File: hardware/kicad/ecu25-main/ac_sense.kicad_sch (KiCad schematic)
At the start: 82 parts, among them J5 Screw_Terminal_GEN, J6 Screw_Terminal_MAINS, J7 Screw_Terminal_CT, U10 MCP6002, U8 MCP6002, U9 MCP6002

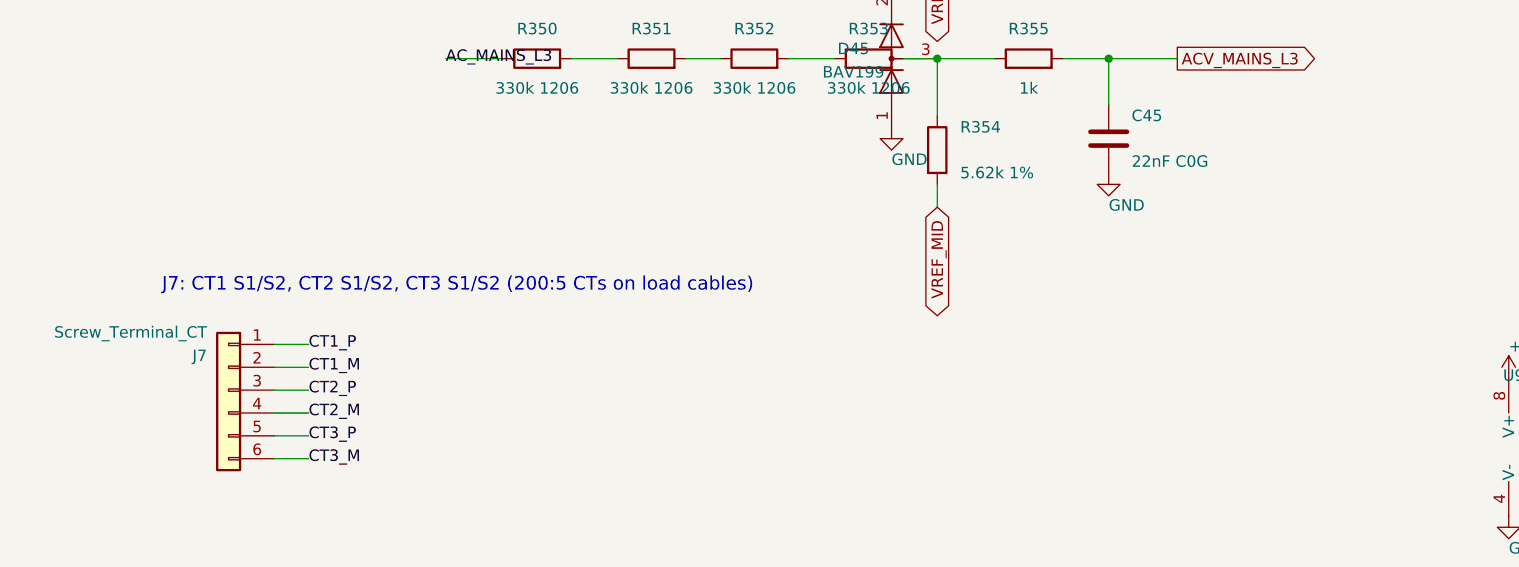
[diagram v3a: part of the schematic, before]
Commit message: Fix firmware SME findings: two criticals in the AC/Modbus interaction
Both criticals needed two modules read together to see.

C1 — a routine Modbus poll could start the engine.
plat_rs485_tx() busy-waited on TXE/TC for the whole response: 26.6 ms for the
51-byte reply to a full input-register read at 19200 baud. The main loop is
the only thing draining the ADC ring, and the ring held 8 sets = 2.5 ms, so
it lapped ten times over with no overrun flag. ac_sense indexes zero
crossings by SAMPLE NUMBER, so a hole in the stream reads as time that did
not pass and comes straight out as a frequency error: a master reading all 23
registers at 10 Hz pinned mains_hz at 53.3 Hz, outside amf_mains_healthy()'s
47-53 window, on every tick. After mains_fail_qualify_ms the controller
declares a mains failure, starts the engine and transfers load. A 12.5 ms
hole crosses the generator frequency trips in both directions.

Fixed three ways, because any one alone is a single point of failure:
- USART3 TX is interrupt-driven; DE still drops on TC, not TXE
- the ring is 64 sets (20 ms) instead of 8
- DMA transfer-complete now counts wraps, so overrun is DETECTABLE (NDTR
  alone is an index and cannot tell "empty" from "lapped exactly once"), and
  the runtime discards the part-built window rather than publishing a
  confidently wrong frequency

C2 — a shorted coolant sender silently deleted the over-temperature
shutdown. On an NTC, a short to the block and a boiling engine are the same
direction. The curve called anything below half the bottom point invalid;
protection.c gates the analog high-temperature check on coolant validity; and
coolant was not in sensors_lost. So a chafed sender wire removed the
shutdown and raised nothing at all. Which end of a curve is a FAULT is now
declared per curve (SENSOR_FAULT_LOW/HIGH) rather than inferred from its
shape, an NTC short stays valid and reads hot, and an invalid coolant reading
raises SENSOR_LOSS.

Majors:
- CAN1 ran with ABOM clear. With K1 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
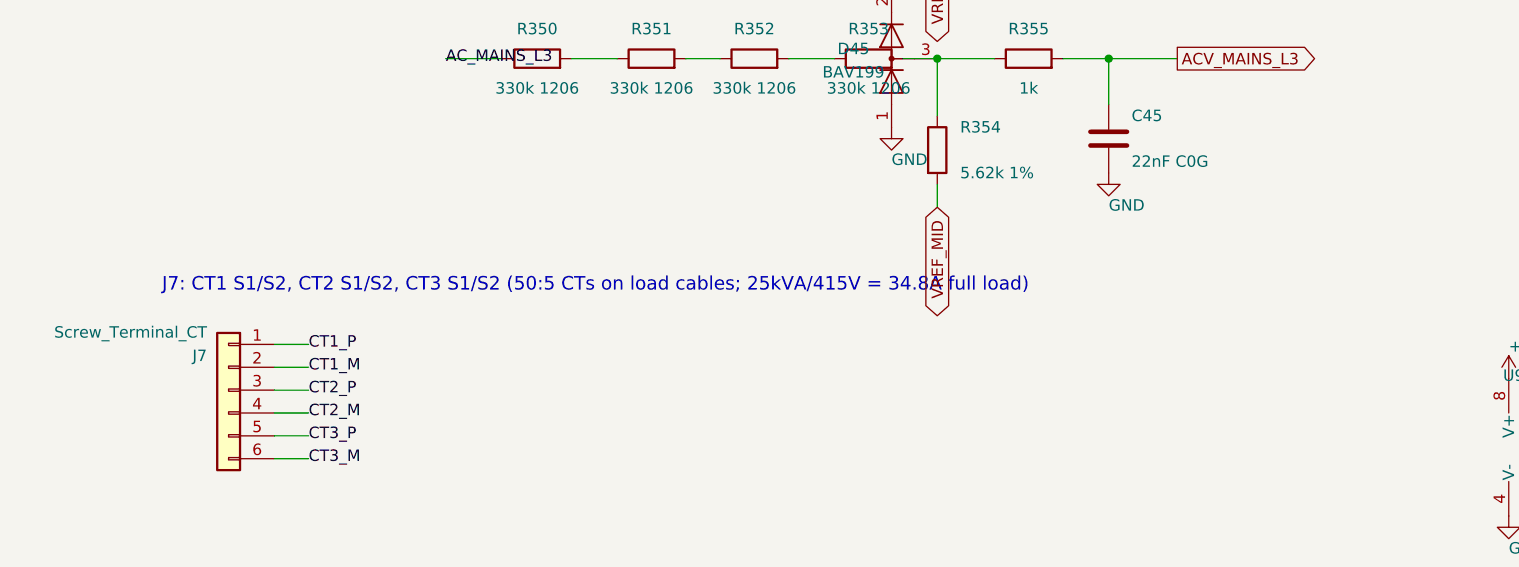
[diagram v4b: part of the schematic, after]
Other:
- note added: "J7: CT1 S1/S2, CT2 S1/S2, CT3 S1/S2 (50:5 CTs on load cables; 25kVA/415V = 34.8A full load)"
- note removed: "J7: CT1 S1/S2, CT2 S1/S2, CT3 S1/S2 (200:5 CTs on load cables)"
